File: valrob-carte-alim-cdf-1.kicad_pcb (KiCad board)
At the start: 4 copper layers, 87 x 57 mm, 201 parts, among them J1 USB_C_Receptacle_USB2.0_14P, J10 Conn_01x02, J11 Conn_01x02, J12 Conn_01x02, J13 Conn_01x02, J14 Conn_01x02, J15 Conn_01x02, J16 Conn_01x02, J17 Conn_01x02, J18 Conn_01x02, J19 Conn_01x02, J2 Conn_01x02, J20 Conn_01x02, J21 Conn_01x02, J22 Conn_01x02, J3 Conn_01x04_Pin, J4 Conn_01x02, J5 Conn_01x02, J6 Conn_01x02, J7 Conn_01x02, J8 Conn_01x02, J9 Conn_01x02, SW1 SW_Push, SW2 SW_Push, SW3 SW_Push, U1 SN65HVD230, U10 TPS259472A, U11 TPS259472A, U12 TPS259472A, U2 ESP32-S3-WROOM-1, U3 TLV75733PDBV, U4 TPS56A37, U5 TPS56A37, U6 TPS259472A, U7 TPS259472A, U8 TPS259472A, U9 TPS259472A

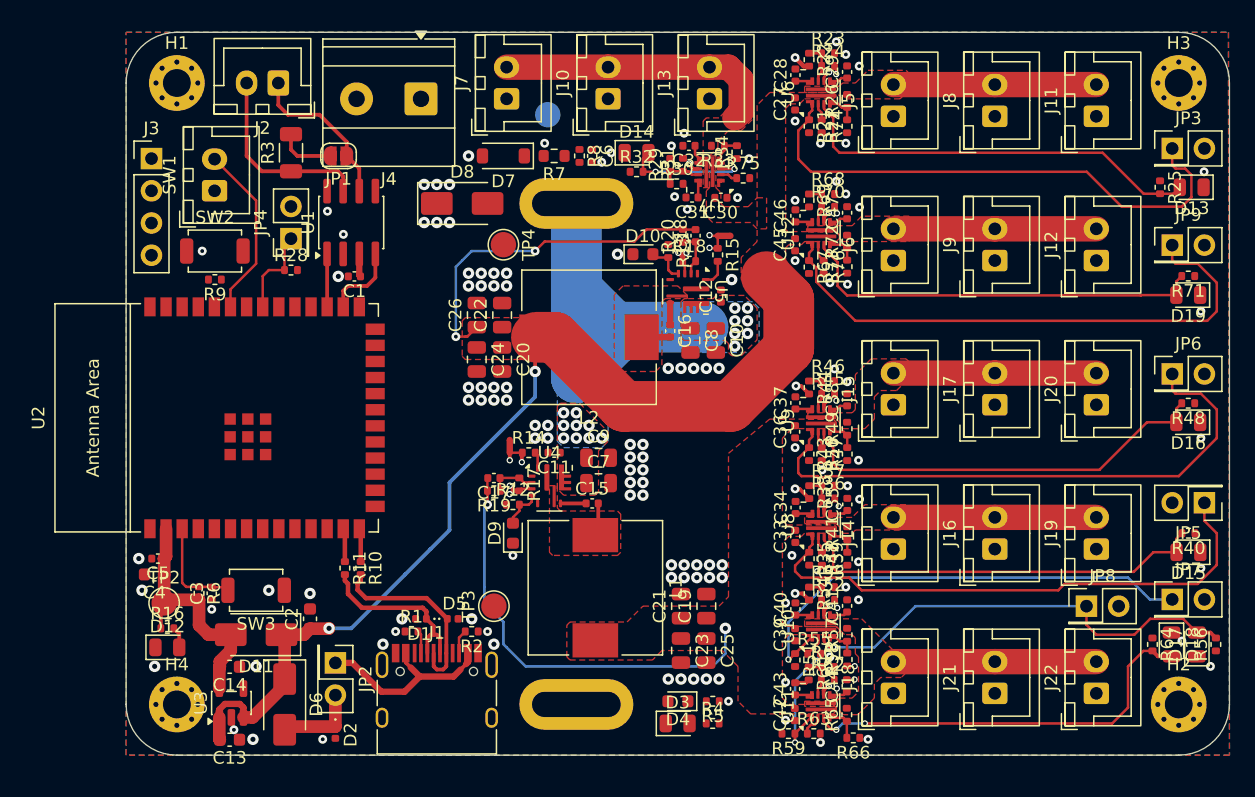
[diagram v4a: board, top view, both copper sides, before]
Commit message: pcb: add efuses' PG AND EN routing
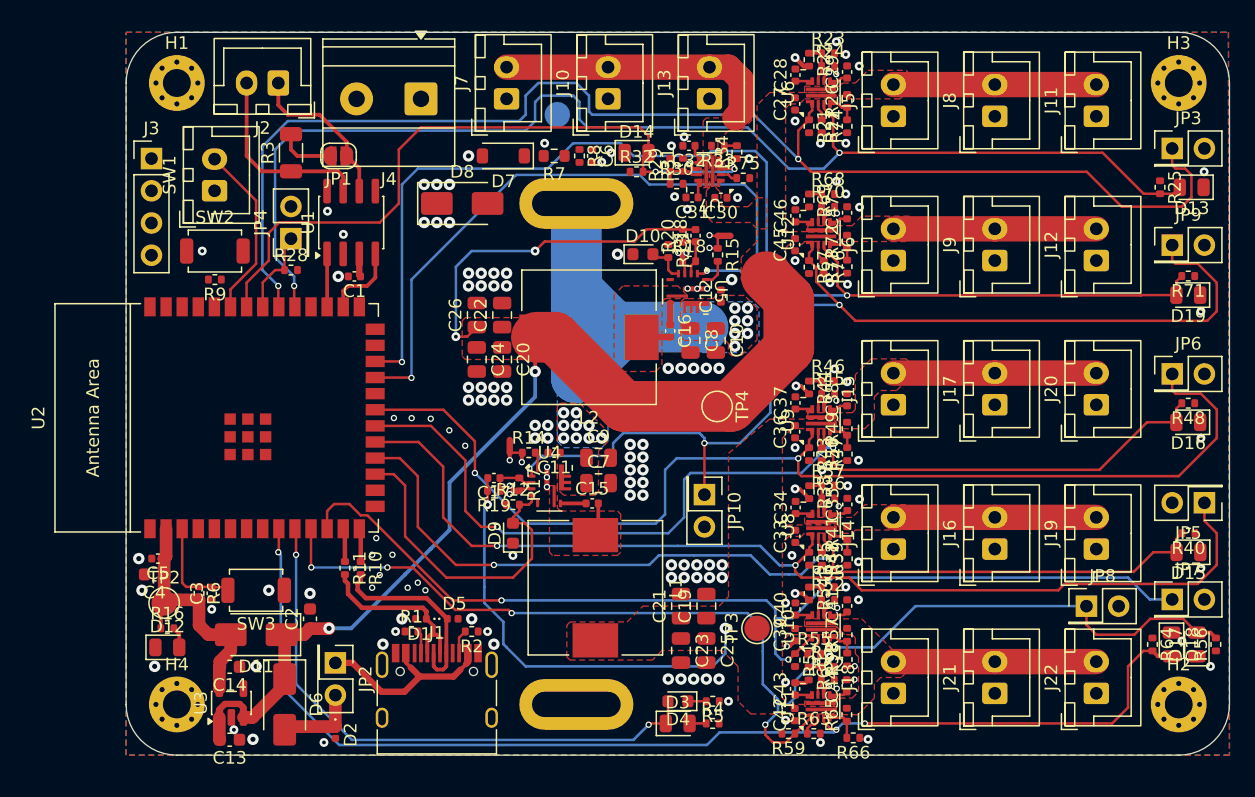
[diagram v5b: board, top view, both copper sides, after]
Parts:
- added JP10: Jumper_2_Small_Open, Connector_PinHeader_2.54mm:PinHeader_2x01_P2.54mm_Vertical, F.Cu at (135.6, 89.5)
- moved TP4 21.1 mm to (136.6, 82.5)
- moved TP3 20.8 mm to (139.8, 100.0)
- moved TP1 0.75 mm to (124.0, 59.5)
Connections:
- U2 pad 10: PG_12V_4 -> Net-(D3-K)
- U2 pad 23: PG_5V_2 -> EN_5V_2
- U2 pad 24: EN_5V_2 -> PG_5V_2
- U2 pad 9: Net-(D3-K) -> PG_12V_4
- U4 pad 1: unconnected-(U4-EN-Pad1) -> /Power/EN
- U5 pad 1: unconnected-(U5-EN-Pad1) -> /Power/EN
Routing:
- net PG_5V_1: track 32.7 -> 96.6 mm, vias 0 -> 2
- net PG_5V_2: track 32.4 -> 94.7 mm, vias 0 -> 2
- net EN_5V_1: track 42.6 -> 104.2 mm, vias 0 -> 2
- net PG_12V_4: track 32.7 -> 91.4 mm, vias 2 -> 3
- net EN_5V_2: track 44.1 -> 99.2 mm, vias 0 -> 2
- net PG_12V_3: track 47.2 -> 97.3 mm, vias 2 -> 5
- net PG_12V_2: track 33.3 -> 79.8 mm, vias 0 -> 2
- net Net-(D3-K): track 0.00 -> 45.6 mm, vias 0 -> 2
- net PG_5V_3: track 10.1 -> 54.1 mm
- net PG_12V_1: track 32.3 -> 75.7 mm, vias 0 -> 2
- net EN_12V_3: track 38.0 -> 81.0 mm, vias 1 -> 2
- net EN_12V_2: track 45.8 -> 88.6 mm, vias 0 -> 2
- net /Power/EN: track 0.00 -> 42.4 mm, vias 0 -> 3
- net EN_12V_1: track 43.4 -> 82.9 mm, vias 0 -> 2
- net /PG_12V: track 3.26 -> 25.9 mm
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
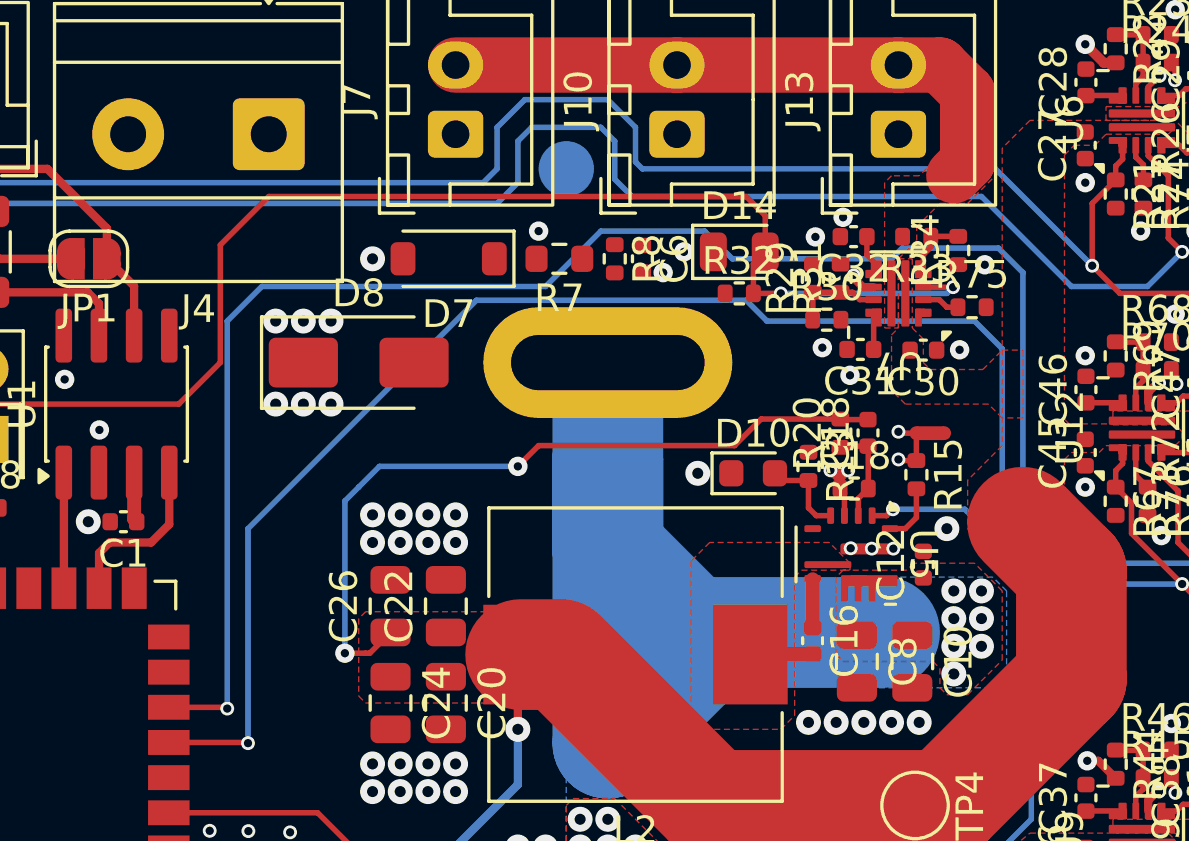
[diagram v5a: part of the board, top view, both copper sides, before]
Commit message: pcb: add vsense routing
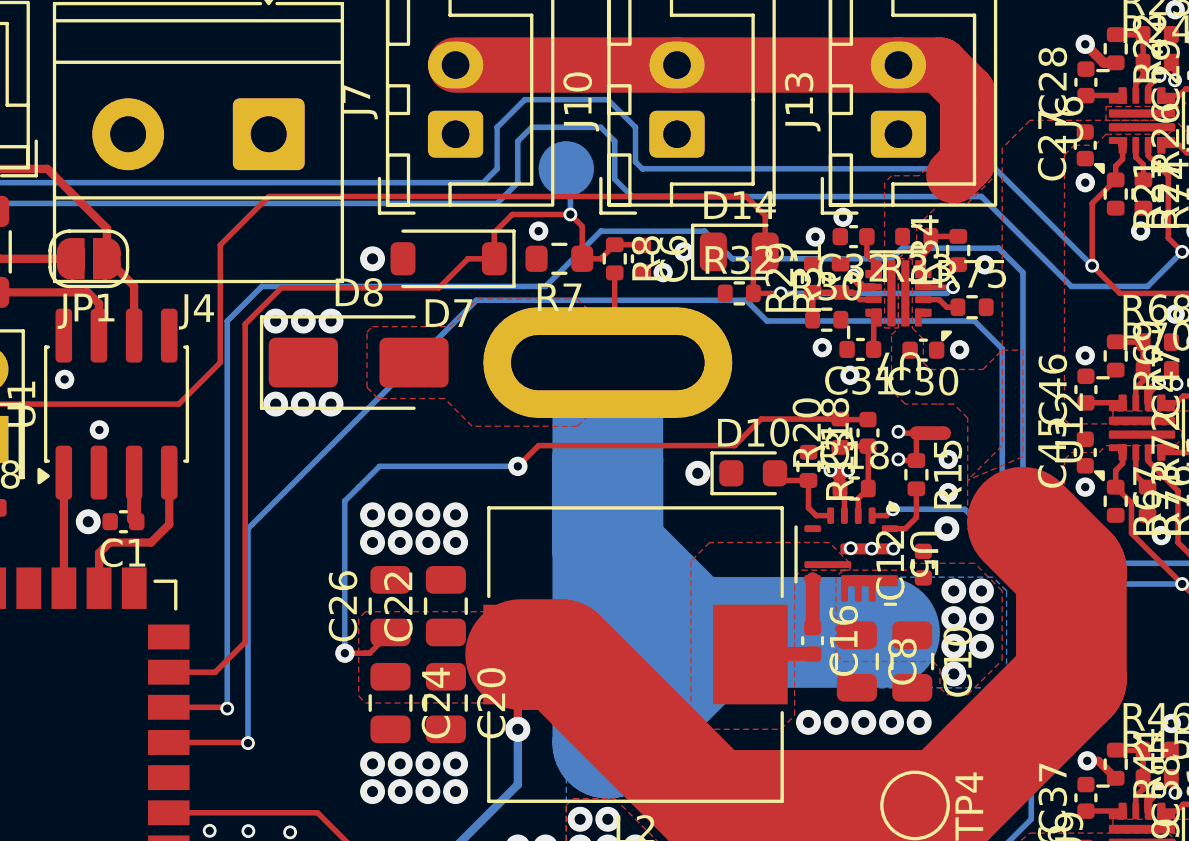
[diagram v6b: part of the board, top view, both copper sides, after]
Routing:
- net /Vsense: track 0.00 -> 34.5 mm, vias 0 -> 1
- net +BATT: track 33.5 -> 36.8 mm
- net GND: vias 166 -> 168
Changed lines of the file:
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@@
 	)
 	(via
+		(at 137.8 70)
+		(size 0.7)
+		(drill 0.3)
+		(layers "F.Cu" "B.Cu")
+		(free yes)
+		(net 1)
+	)
+	(via
 		(at 130.75 86.5)
 		(size 0.9)
@@
 	)
 	(via
+		(at 137.8 71.2)
+		(size 0.7)
+		(drill 0.3)
+		(layers "F.Cu" "B.Cu")
+		(free yes)
+		(net 1)
+	)
+	(via
 		(at 119 72)
 		(size 0.9)
@@
 		(net 1)
 	)
+	(segment
+		(start 125.75 63.26)
+		(end 125.75 66.25)
+		(width 0.2)
+		(layer "F.Cu")
+		(net 2)
+	)
+	(segment
+		(start 125.75 66.25)
+		(end 125.5 66.5)
+		(width 0.2)
+		(layer "F.Cu")
+		(net 2)
+	)
 	(via
 		(at 139 74.75)
@@
 	)
 	(segment
+		(start 121.4 62.75)
+		(end 121.4 61.8)
+		(width 0.2)
+		(layer "F.Cu")
+		(net 6)
+	)
+	(segment
+		(start 125.24 62.75)
+		(end 125.75 62.24)
+		(width 0.2)
+		(layer "F.Cu")
+		(net 6)
+	)
+	(segment
+		(start 125.75 62.24)
+		(end 126.72 62.24)
+		(width 0.2)
+		(layer "F.Cu")
+		(net 6)
+	)
+	(segment
+		(start 109.64 77.685)
+		(end 111.315 77.685)
+		(width 0.2)
+		(layer "F.Cu")
+		(net 6)
+	)
+	(segment
+		(start 120.45 62.75)
+		(end 121.4 62.75)
+		(width 0.2)
+		(layer "F.Cu")
+		(net 6)
+	)
+	(segment
+		(start 124.575 61.575)
+		(end 124.575 62.75)
+		(width 0.2)
+		(layer "F.Cu")
+		(net 6)
+	)
+	(segment
+		(start 126.72 62.24)
+		(end 126.75 62.27)
+		(width 0.2)
+		(layer "F.Cu")
+		(net 6)
+	)
+	(segment
+		(start 113.708636 63.8)
+		(end 119.4 63.8)
+		(width 0.2)
+		(layer "F.Cu")
+		(net 6)
+	)
+	(segment
+		(start 112.4 76.6)
+		(end 112.4 65.108636)
+		(width 0.2)
+		(layer "F.Cu")
+		(net 6)
+	)
+	(segment
+		(start 124.575 62.75)
+		(end 125.24 62.75)
+		(width 0.2)
+		(layer "F.Cu")
+		(net 6)
+	)
+	(segment
+		(start 112.4 65.108636)
+		(end 113.708636 63.8)
+		(width 0.2)
+		(layer "F.Cu")
+		(net 6)
+	)
+	(segment
+		(start 122.051 61.149)
+		(end 124.149 61.149)
+		(width 0.2)
+		(layer "F.Cu")
+		(net 6)
+	)
+	(segment
+		(start 124.149 61.149)
+		(end 124.575 61.575)
+		(width 0.2)
+		(layer "F.Cu")
+		(net 6)
+	)
+	(segment
+		(start 111.315 77.685)
+		(end 112.4 76.6)
+		(width 0.2)
+		(layer "F.Cu")
+		(net 6)
+	)
+	(segment
+		(start 119.4 63.8)
+		(end 120.45 62.75)
+		(width 0.2)
+		(layer "F.Cu")
+		(net 6)
+	)
+	(segment
+		(start 121.4 61.8)
+		(end 122.051 61.149)
+		(width 0.2)
+		(layer "F.Cu")
+		(net 6)
+	)
+	(via
+		(at 124.149 61.149)
+		(size 0.5)
+		(drill 0.3)
+		(layers "F.Cu" "B.Cu")
+		(net 6)
+	)
+	(segment
+		(start 124.149 59.649)
+		(end 124 59.5)
+		(width 0.2)
+		(layer "B.Cu")
+		(net 6)
+	)
+	(segment
+		(start 124.149 61.149)
+		(end 124.149 59.649)
+		(width 0.2)
+		(layer "B.Cu")
+		(net 6)
+	)
+	(segment
 		(start 127.23 90.15)
 		(end 127.23 92.42)
@@
 		(polygon
 			(pts
-				(xy 139.75 68.5) (xy 139.25 68) (xy 136.25 68) (xy 135.75 67.5) (xy 135.75 65.5) (xy 136 65.25)
-				(xy 136 62.75) (xy 136.5 62.75) (xy 136.5 65.25) (xy 136.9 65.65) (xy 136.9 66.5) (xy 137.15 66.75)
-				(xy 139.05 66.75) (xy 139.75 66.05) (xy 140.5 66.05) (xy 140.5 68.5)
+				(xy 138.5 70.75) (xy 138.504825 68.511793) (xy 138 68) (xy 137.4 68) (xy 136.25 68) (xy 135.75 67.5)
+				(xy 135.75 65.5) (xy 136 65.25) (xy 136 62.75) (xy 136.5 62.75) (xy 136.5 65.25) (xy 136.9 65.65)
+				(xy 136.9 66.5) (xy 137.15 66.75) (xy 139.05 66.75) (xy 139.75 66.05) (xy 140.5 66.05) (xy 140.5 69.9)
 			)
 		)
@@
 			)
 		)
+	)
+	(zone
+		(net 2)
+		(net_name "+BATT")
+		(layer "F.Cu")
+		(hatch edge 0.5)
+		(priority 17)
+		(connect_pads yes
+			(clearance 0.2)
+		)
+		(min_thickness 0.25)
+		(filled_areas_thickness no)
+		(fill yes
+			(thermal_gap 0.5)
+			(thermal_bridge_width 0.5)
+		)
+		(polygon
+			(pts
+				(xy 117.2 67.8) (xy 116.8 67.4) (xy 116.8 65.4) (xy 117 65.2) (xy 119.8 65.2) (xy 120.8 64.2) (xy 124.4 64.2)
+				(xy 124.8 64.6) (xy 124.8 68.4) (xy 124.4 68.8) (xy 120.6 68.8) (xy 119.6 67.8) (xy 117.4 67.8)
+			)
+		)

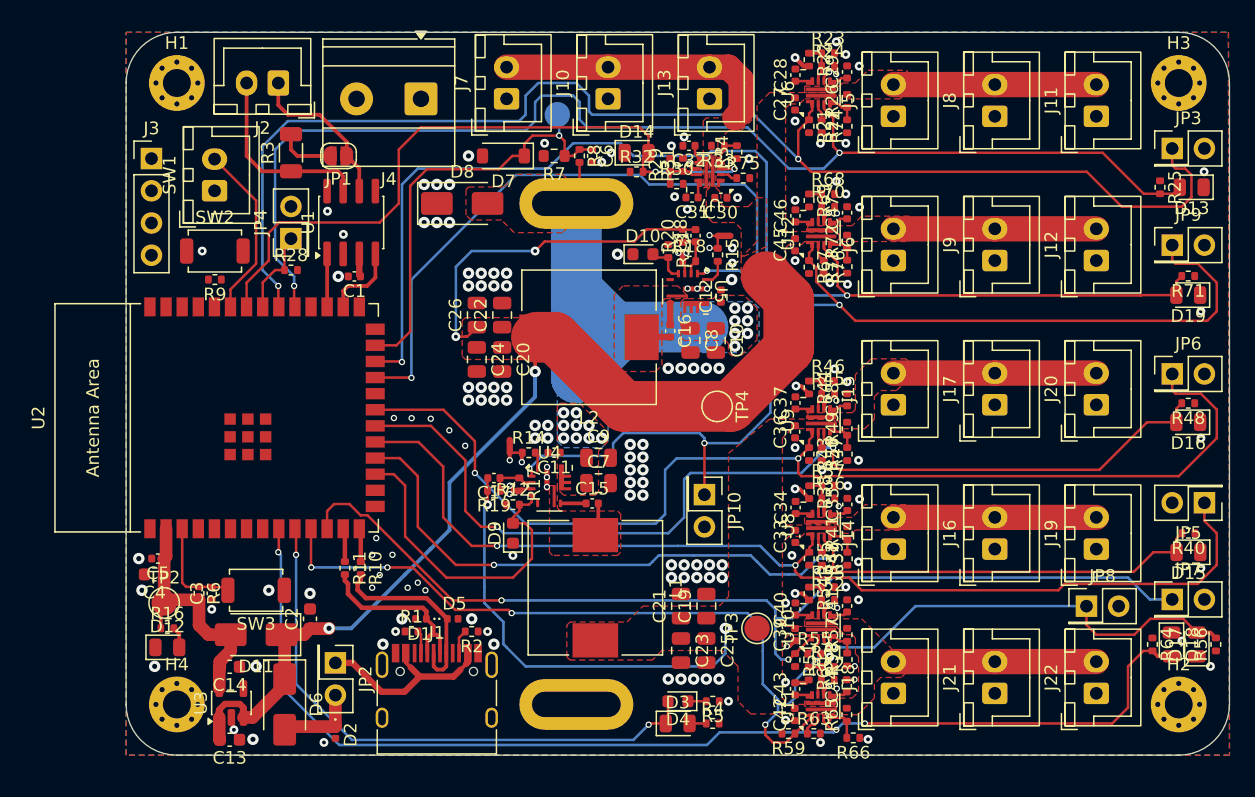
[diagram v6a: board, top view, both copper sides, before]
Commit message: pcb: add efuses ILM routing
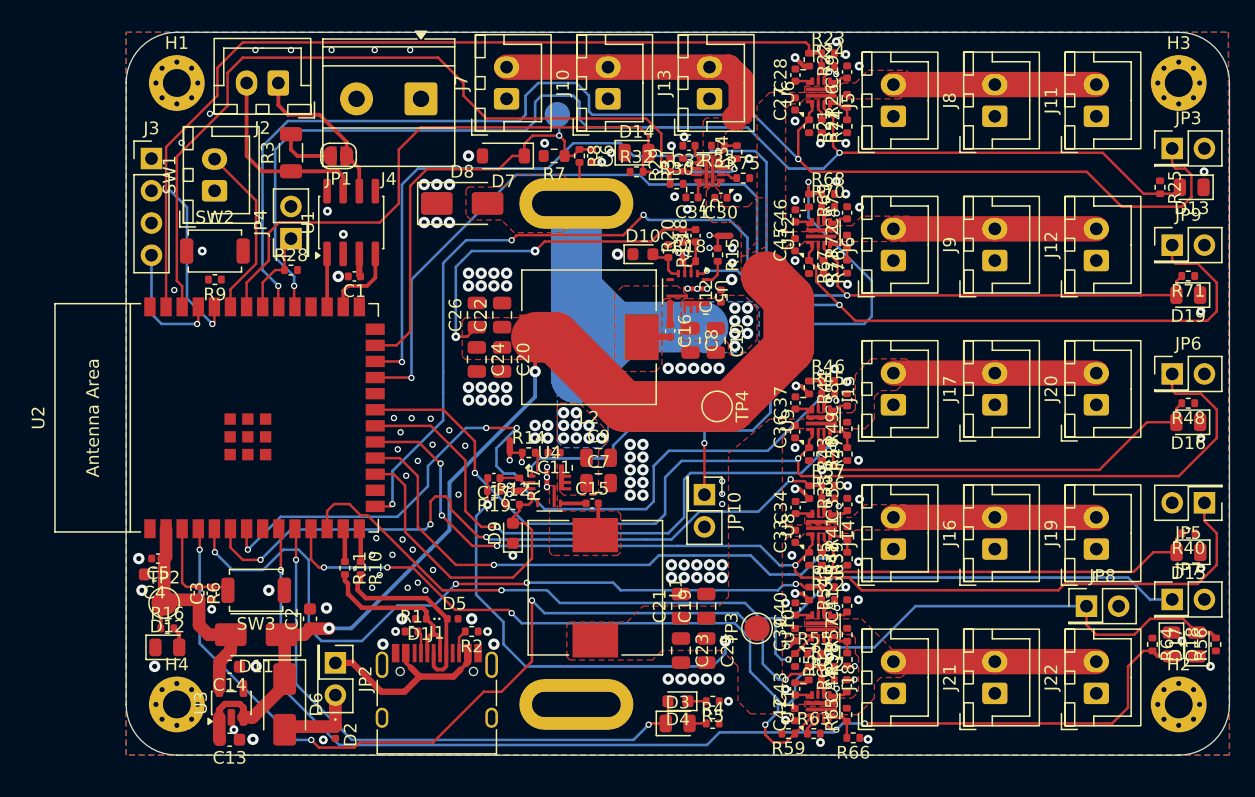
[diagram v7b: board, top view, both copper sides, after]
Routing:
- net ILM_5V_2: track 3.29 -> 79.5 mm, vias 0 -> 4
- net ILM_12V_4: track 3.29 -> 75.6 mm, vias 0 -> 4
- net ILM_5V_1: track 3.29 -> 72.0 mm
- net ILM_12V_2: track 3.29 -> 70.0 mm, vias 0 -> 4
- net ILM_5V_3: track 3.29 -> 64.7 mm
- net ILM_12V_3: track 3.29 -> 61.9 mm, vias 0 -> 4
- net ILM_12V_1: track 3.29 -> 57.9 mm, vias 0 -> 4
- net /U0RXD: track 0.00 -> 14.8 mm, vias 0 -> 1
- net /U0TXD: track 0.00 -> 9.94 mm, vias 0 -> 1
- net PG_12V_3: track 97.3 -> 95.9 mm
- net GND: vias 168 -> 188
- net EN_12V_1: vias 2 -> 4
